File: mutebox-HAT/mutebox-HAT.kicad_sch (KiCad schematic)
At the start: 6 parts, among them J1 GPIO, U1 CAT24C256

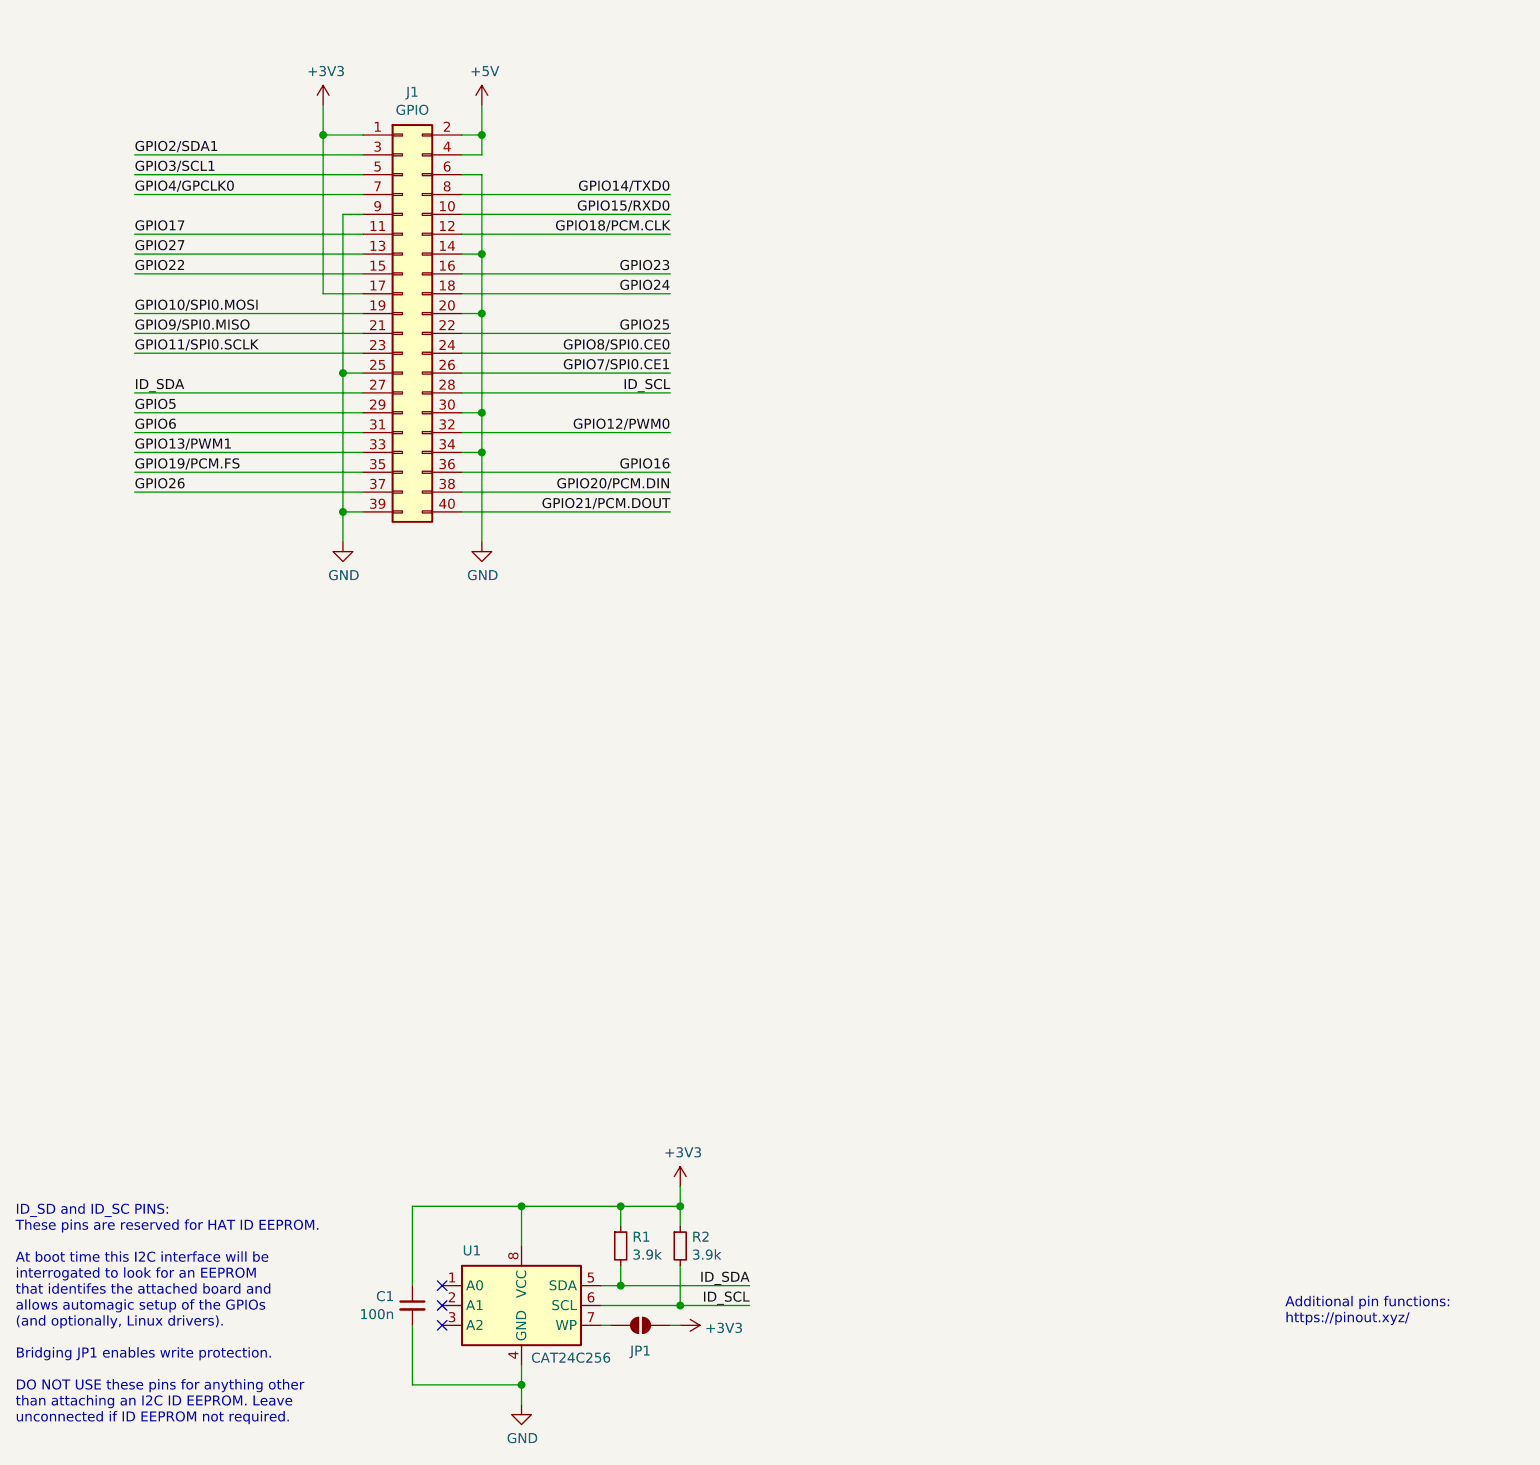
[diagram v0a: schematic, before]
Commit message: Added chips to support RCA and digital audio input
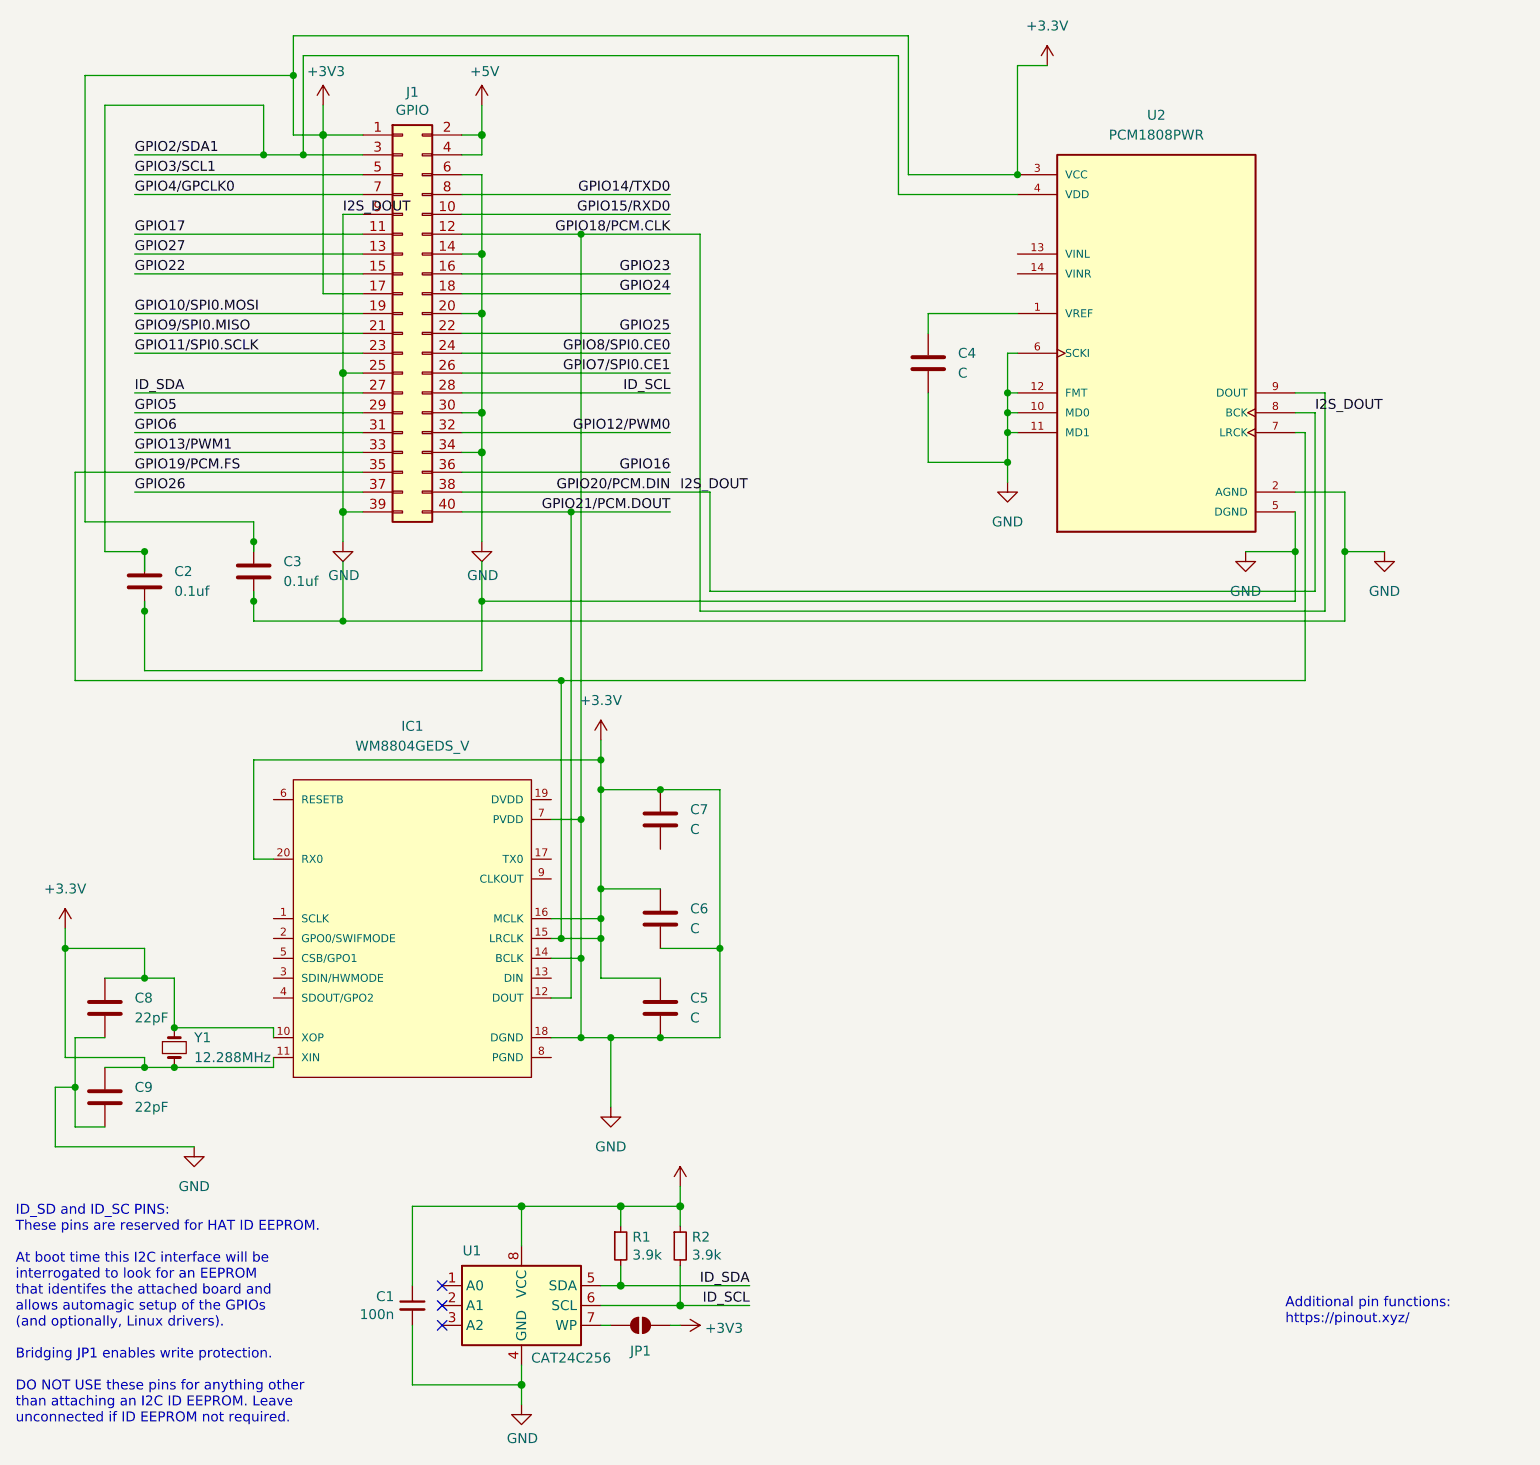
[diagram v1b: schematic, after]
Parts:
- added C2, C3: 0.1uf, symbol Device:C
- added C4, C5, C6, C7: C, symbol Device:C
- added C8, C9: 22pF, symbol Device:C
- added IC1: WM8804GEDS_V, WM8804GEDS_V:SOP65P780X200-20N, symbol WM8804GEDS_V:WM8804GEDS_V
- added U2: PCM1808PWR, PCM1808PWR:SOP65P640X120-14N, symbol PCM1808PWR:PCM1808PWR
- added Y1: 12.288MHz, symbol Device:Crystal_Small
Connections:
- net GND is gone; now on net +3.3V: C1.2, J1.14 (Pin_14), J1.20 (Pin_20), J1.25 (Pin_25), J1.30 (Pin_30), J1.34 (Pin_34), J1.39 (Pin_39), J1.6 (Pin_6), J1.9 (Pin_9), U1.4 (GND)
- net GPIO18/PCM.CLK is gone; now on net +3.3V: J1.12 (Pin_12)
- net GPIO19/PCM.FS is gone; now on net +3.3V: J1.35 (Pin_35)
- net GPIO20/PCM.DIN is gone; now on net +3.3V: J1.38 (Pin_38)
- net GPIO21/PCM.DOUT: now also IC1.12 (DOUT)
- net GPIO2/SDA1: now also C2.1, U2.4 (VDD)
- net +3V3 renamed +3.3V
- net +3.3V: now also C2.2, C3.1, C3.2, C4.2, C5.1, C5.2, C6.1, C6.2, C7.1, C8.1, C8.2, C9.1, C9.2, IC1.10 (XOP), IC1.11 (XIN), IC1.14 (BCLK), IC1.15 (LRCLK), IC1.16 (MCLK), IC1.18 (DGND), IC1.20 (RX0), IC1.7 (PVDD), U2.10 (MD0), U2.11 (MD1), U2.12 (FMT), U2.2 (AGND), U2.3 (VCC), U2.5 (DGND), U2.6 (SCKI), U2.7 (LRCK), U2.8 (BCK), U2.9 (DOUT), Y1.1, Y1.2
- new net: C4.1, U2.1 (VREF)
